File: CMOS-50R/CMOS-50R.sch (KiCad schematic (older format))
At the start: 43 parts, among them J1 Conn_01x06_Male, J11 Conn_Coaxial, J21 Conn_Coaxial, J31 Conn_Coaxial, J41 Conn_Coaxial, U1 7404, U2 7404, U3 7404, U4 7404

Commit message: Added fiducials and mounting hole
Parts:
- added FID1, FID2, FID3, FID4: Fiducial, Fiducial:Fiducial_1mm_Mask2mm, symbol Mechanical:Fiducial
- added H1: MountingHole_Pad, MountingHole:MountingHole_3.5mm_Pad_Via, symbol Mechanical:MountingHole_Pad
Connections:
- net GND: now also H1.1
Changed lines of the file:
@@
 Wire Wire Line
 	1600 1100 1950 1100
+$Comp
+L Mechanical:Fiducial FID1
+U 1 1 5D69365C
+P 4850 6650
+F 0 "FID1" H 4935 6696 50  0000 L CNN
+F 1 "Fiducial" H 4935 6605 50  0000 L CNN
+F 2 "Fiducial:Fiducial_1mm_Mask2mm" H 4850 6650 50  0001 C CNN
+F 3 "~" H 4850 6650 50  0001 C CNN
+	1    4850 6650
+	1    0    0    -1
+$EndComp
+$Comp
+L Mechanical:Fiducial FID3
+U 1 1 5D698780
+P 5450 6650
+F 0 "FID3" H 5535 6696 50  0000 L CNN
+F 1 "Fiducial" H 5535 6605 50  0000 L CNN
+F 2 "Fiducial:Fiducial_1mm_Mask2mm" H 5450 6650 50  0001 C CNN
+F 3 "~" H 5450 6650 50  0001 C CNN
+	1    5450 6650
+	1    0    0    -1
+$EndComp
+$Comp
+L Mechanical:Fiducial FID2
+U 1 1 5D698B98
+P 4850 6900
+F 0 "FID2" H 4935 6946 50  0000 L CNN
+F 1 "Fiducial" H 4935 6855 50  0000 L CNN
+F 2 "Fiducial:Fiducial_1mm_Mask2mm" H 4850 6900 50  0001 C CNN
+F 3 "~" H 4850 6900 50  0001 C CNN
+	1    4850 6900
+	1    0    0    -1
+$EndComp
+$Comp
+L Mechanical:Fiducial FID4
+U 1 1 5D699013
+P 5450 6900
+F 0 "FID4" H 5535 6946 50  0000 L CNN
+F 1 "Fiducial" H 5535 6855 50  0000 L CNN
+F 2 "Fiducial:Fiducial_1mm_Mask2mm" H 5450 6900 50  0001 C CNN
+F 3 "~" H 5450 6900 50  0001 C CNN
+	1    5450 6900
+	1    0    0    -1
+$EndComp
+$Comp
+L Mechanical:MountingHole_Pad H1
+U 1 1 5D6999E2
+P 6050 6800
+F 0 "H1" H 6150 6849 50  0000 L CNN
+F 1 "MountingHole_Pad" H 6150 6758 50  0000 L CNN
+F 2 "MountingHole:MountingHole_3.5mm_Pad_Via" H 6050 6800 50  0001 C CNN
+F 3 "~" H 6050 6800 50  0001 C CNN
+	1    6050 6800
+	1    0    0    -1
+$EndComp
+$Comp
+L power:GND #PWR015
+U 1 1 5D6A7408
+P 6050 6900
+F 0 "#PWR015" H 6050 6650 50  0001 C CNN
+F 1 "GND" H 6055 6727 50  0000 C CNN
+F 2 "" H 6050 6900 50  0001 C CNN
+F 3 "" H 6050 6900 50  0001 C CNN
+	1    6050 6900
+	1    0    0    -1
+$EndComp
 $EndSCHEMATC

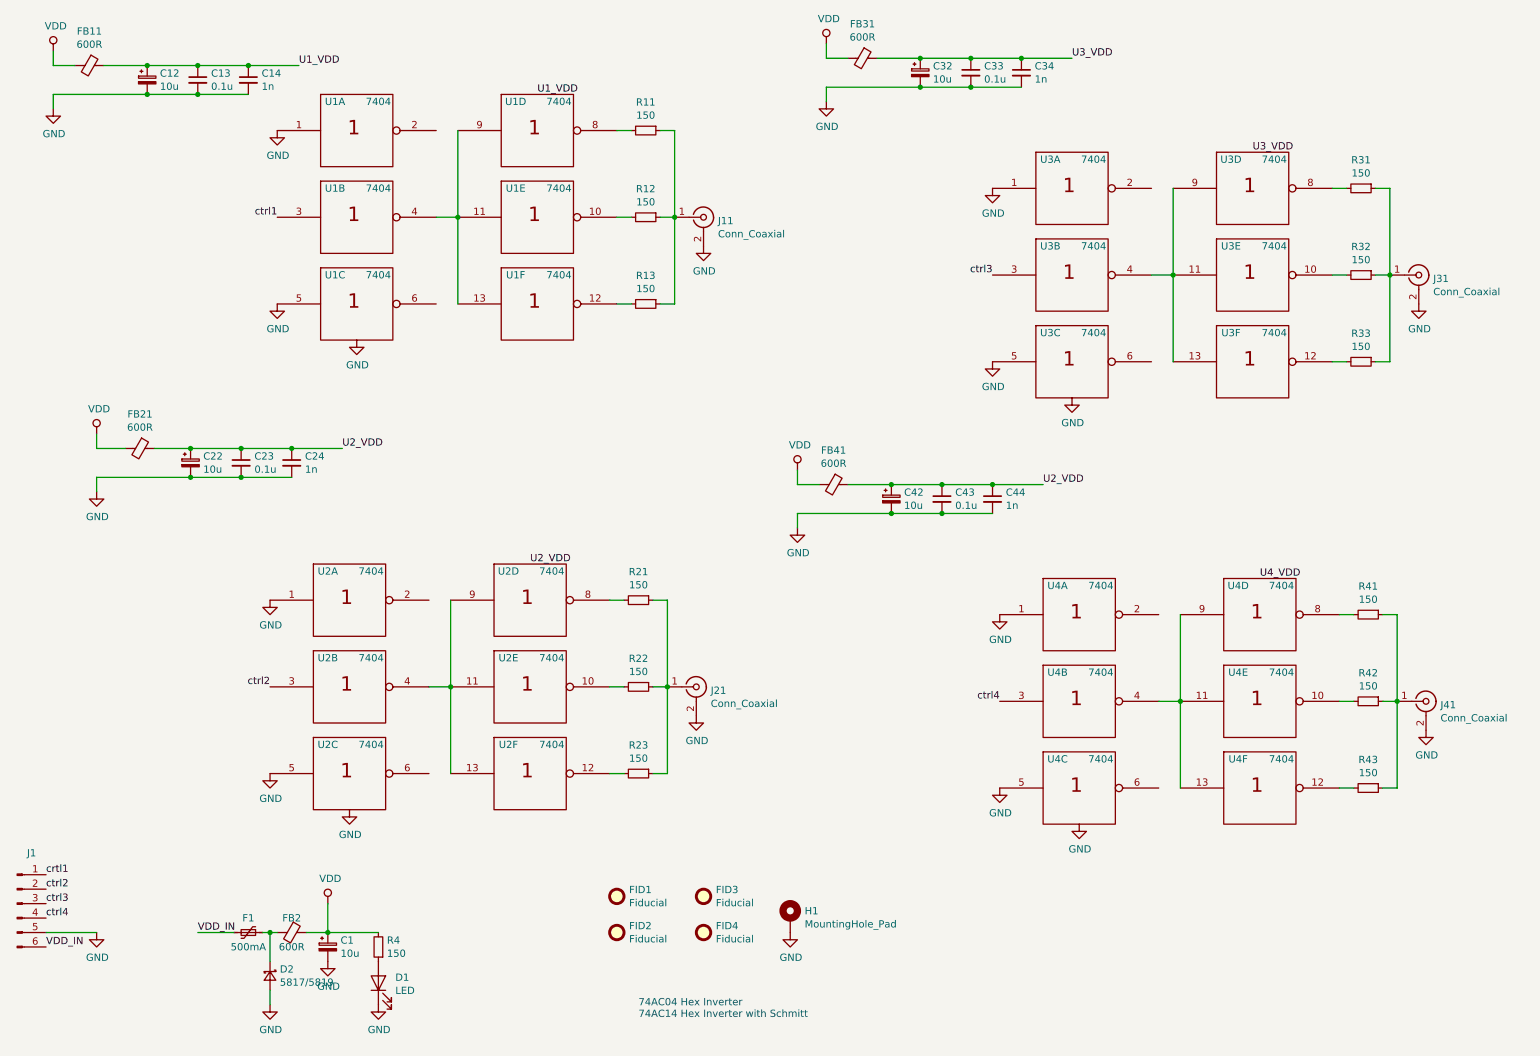
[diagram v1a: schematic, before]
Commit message: First full functional layout trace route
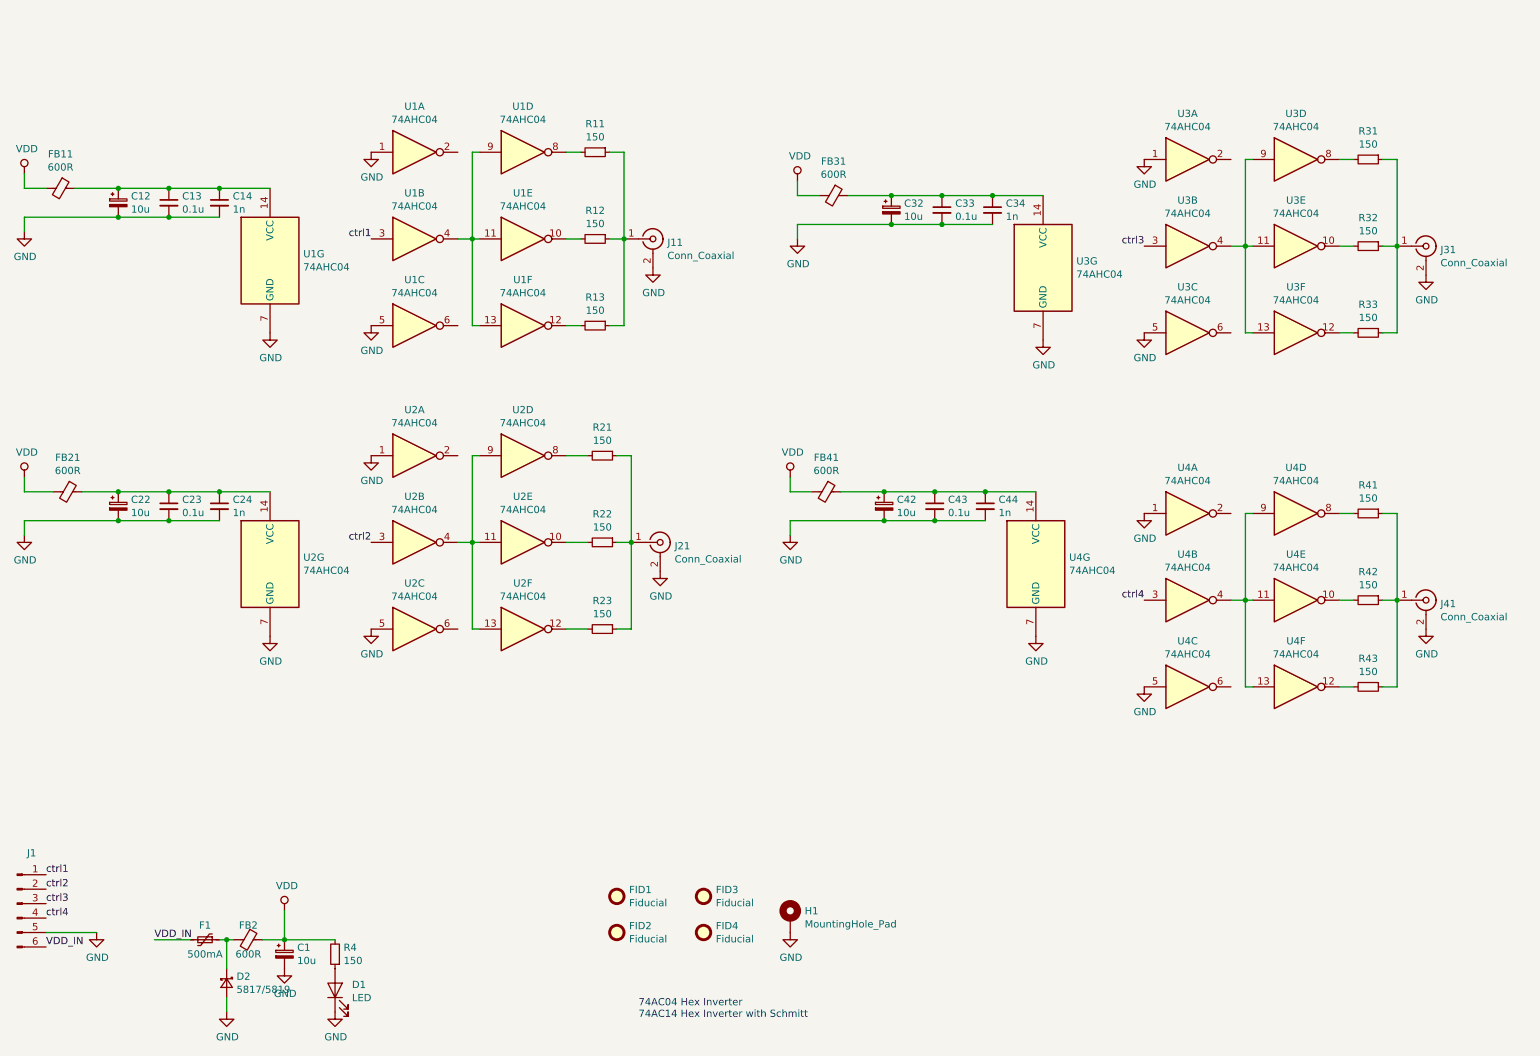
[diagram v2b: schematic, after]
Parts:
- removed U1, U2, U3, U4: 7404, Package_SO:SOIC-14_3.9x8.7mm_P1.27mm, symbol 74xx_IEEE:7404
- added U1, U2, U3, U4: 74AHC04, Package_SO:SOIC-14_3.9x8.7mm_P1.27mm, symbol 74xx:74AHC04
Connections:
- net crtl1 is gone; now on net ctrl1: J1.1 (Pin_1)
- net GND: now also U1.1, U1.5, U1.7 (GND), U2.1, U2.5, U2.7 (GND), U3.1, U3.5, U3.7 (GND), U4.1, U4.5, U4.7 (GND)
- net ctrl1: now also U1.3
- net ctrl2: now also U2.3
- net ctrl3: now also U3.3
- net ctrl4: now also U4.3
- net at R11.2: now also U1.8
- net at R12.2: now also U1.10
- net at R13.2: now also U1.12
- net at R21.2: now also U2.8
- net at R22.2: now also U2.10
- net at R23.2: now also U2.12
- net at R31.2: now also U3.8
- net at R32.2: now also U3.10
- net at R33.2: now also U3.12
- net at R41.2: now also U4.8
- net at R42.2: now also U4.10
- net at R43.2: now also U4.12
- removed net Vcc: C12.1, C13.1, C14.1, C22.1, C23.1, C24.1, C32.1, C33.1, C34.1, C42.1, C43.1, C44.1, FB11.1, FB21.1, FB31.1, FB41.1
- new net: C12.1, C13.1, C14.1, FB11.1, U1.14 (VCC)
- new net: C22.1, C23.1, C24.1, FB21.1, U2.14 (VCC)
- new net: C32.1, C33.1, C34.1, FB31.1, U3.14 (VCC)
- new net: C42.1, C43.1, C44.1, FB41.1, U4.14 (VCC)
- new net: U1.11, U1.13, U1.4, U1.9
- new net: U3.11, U3.13, U3.4, U3.9
- new net: U2.11, U2.13, U2.4, U2.9
- new net: U4.11, U4.13, U4.4, U4.9
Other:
- moved on the sheet: C1, C12, C13, C14, C22, C23, C24, C32, C33, C34, C42, C43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

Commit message: finished annotations
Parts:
- J1: value Conn_01x06_Male -> PMOD
- J11, J21, J31, J41: value Conn_Coaxial -> SMA
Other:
- note added: "NOTES:\nSuitable logic gate integrated circuits are as follows:\n74AC04/74HC04 Hex Inverter\n74AC14/74HC14 Hex Inverter with Schmitt\n\nAcceptable supply voltage: VDD = 3.3v/5v"
- note removed: "74AC04 Hex Inverter\n74AC14 Hex Inverter with Schmitt"
- moved on the sheet: C1, D1, D2, F1, FB2, FID1, FID2, FID3, FID4, H1, J1, R4
